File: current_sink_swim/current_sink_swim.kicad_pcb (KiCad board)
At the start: 2 copper layers, 49.3 x 42.6 mm, 23 parts, among them J1 Conn_01x02_Socket, J2 Conn_01x03_Socket, J3 Conn_01x02_Socket, J4 Conn_01x01_Pin, Q2 IRF540N, U1 LMV358, U3 TC1016

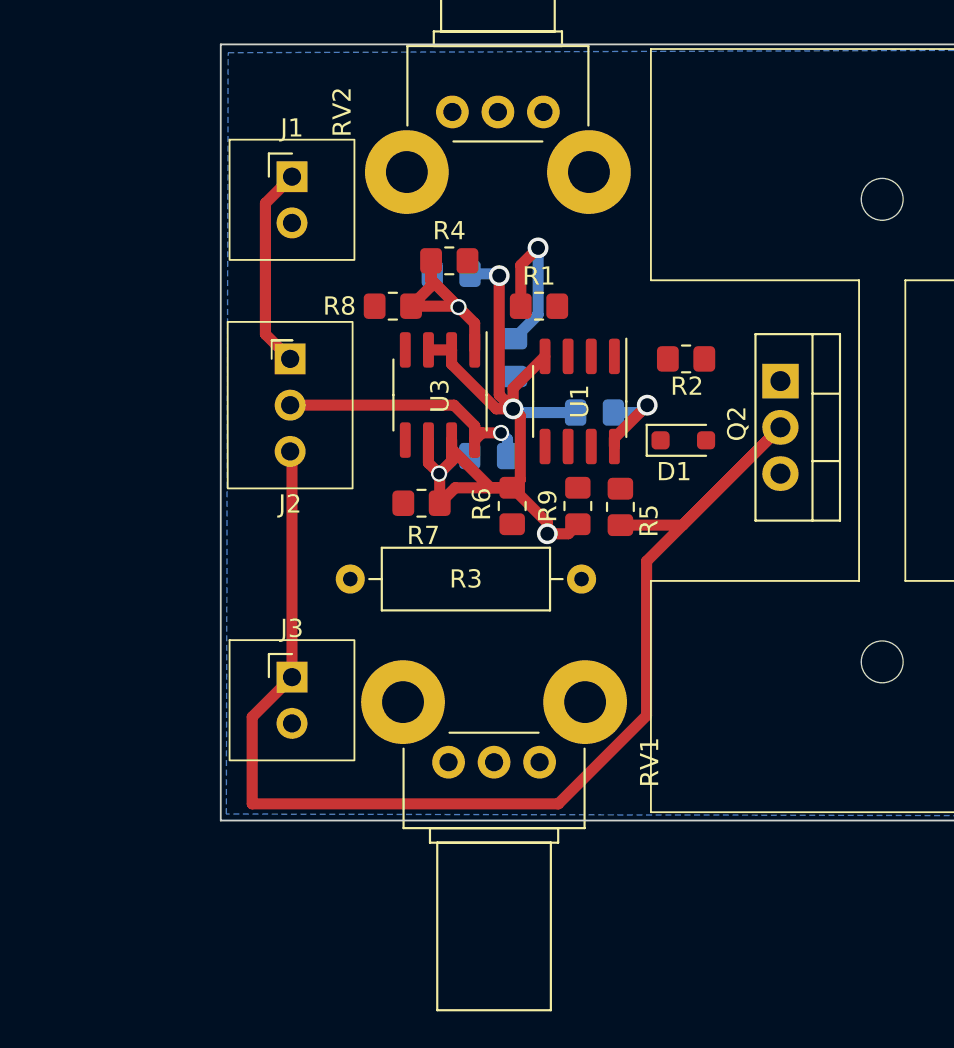
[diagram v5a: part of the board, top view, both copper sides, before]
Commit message: move some componenets around and route all traces
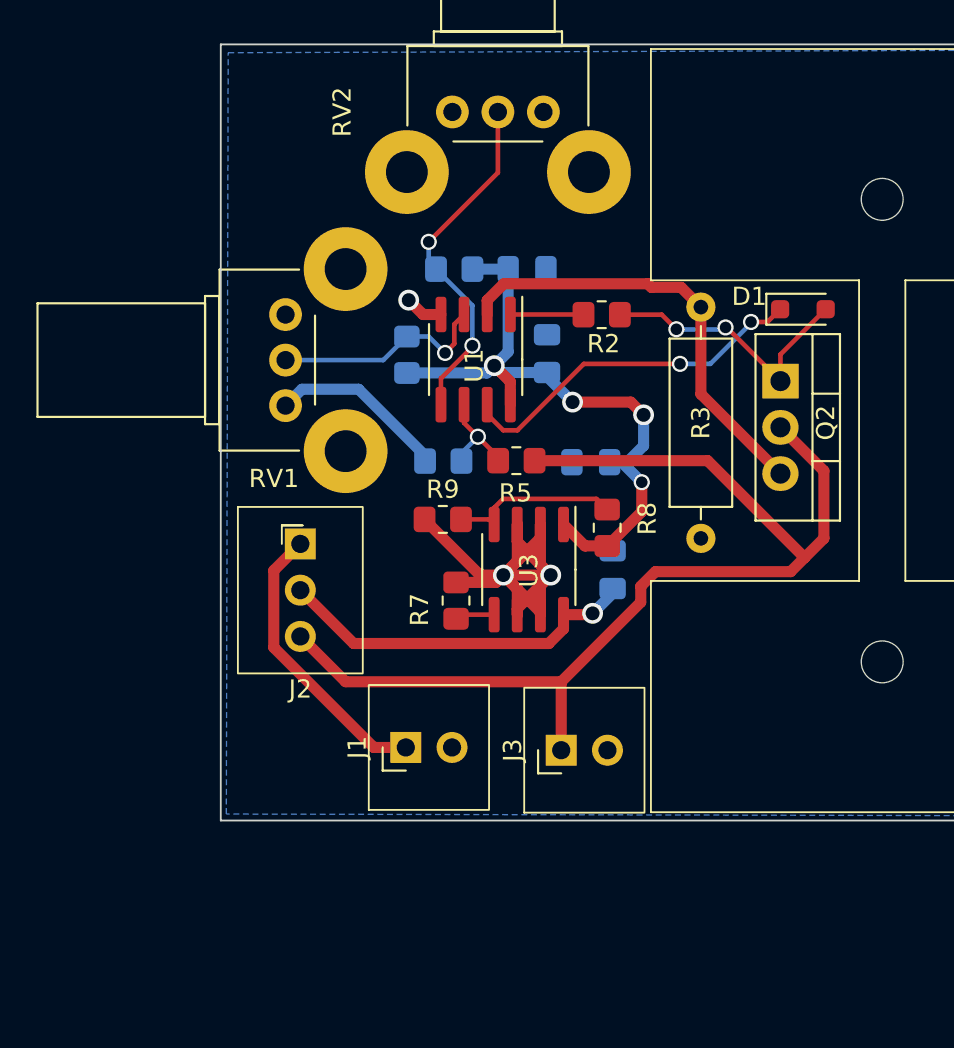
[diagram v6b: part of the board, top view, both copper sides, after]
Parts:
- R1, R4, R6: moved to B.Cu
- moved J1 32.0 mm to (116.9, 67.6), turned to 90 degrees
- moved RV1 26.2 mm to (110.3, 43.8), turned to 180 degrees
- moved R8 16.9 mm to (128.0, 55.5), turned to -90 degrees
- moved R3 16.3 mm to (133.1, 43.4), turned to -90 degrees
- moved J3 15.3 mm to (125.5, 67.7), turned to 90 degrees
- moved U3 10.8 mm to (123.7, 57.8)
- moved J2 10.2 mm to (111.2, 56.4)
- moved D1 9.74 mm to (138.8, 43.5)
- moved C3 9.23 mm to (128.3, 57.8), turned to -90 degrees
- moved R1 7.73 mm to (117.0, 46.0), turned to 90 degrees
- moved R9 7.45 mm to (119.0, 55.0), turned to 0 degrees
- moved C4 7.12 mm to (127.1, 51.9), turned to 0 degrees
- moved R5 6.25 mm to (123.0, 51.8), turned to 180 degrees
- moved U1 6.16 mm to (120.8, 46.3)
- moved R7 5.67 mm to (119.7, 59.5), turned to -90 degrees
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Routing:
- net Net-(Q2-S): track 0.00 -> 24.4 mm
- net Net-(D1-K): track 0.00 -> 19.8 mm, vias 0 -> 2
- net Net-(U1B-+): track 0.00 -> 19.4 mm, vias 0 -> 2
- net / Current Control/FETGate: track 0.00 -> 15.4 mm, vias 0 -> 2
- net Current_Sink+: track 73.9 -> 61.4 mm
- net Net-(U1A-+): track 0.00 -> 12.2 mm, vias 0 -> 1
- net 2.7V: track 28.1 -> 37.8 mm, vias 3 -> 4
- net Net-(U3-ADJ): track 0.00 -> 9.50 mm
- net Vin: track 14.4 -> 20.2 mm
- net Net-(U1B--): track 0.00 -> 5.57 mm, vias 0 -> 1
- net Net-(J1-Pin_1): track 11.2 -> 15.8 mm
- net Current_Sink-: track 51.5 -> 47.0 mm, vias 4 -> 3
- net Net-(R2-Pad1): track 0.00 -> 4.02 mm
- net Net-(U3-INHIBIT): track 0.00 -> 2.19 mm

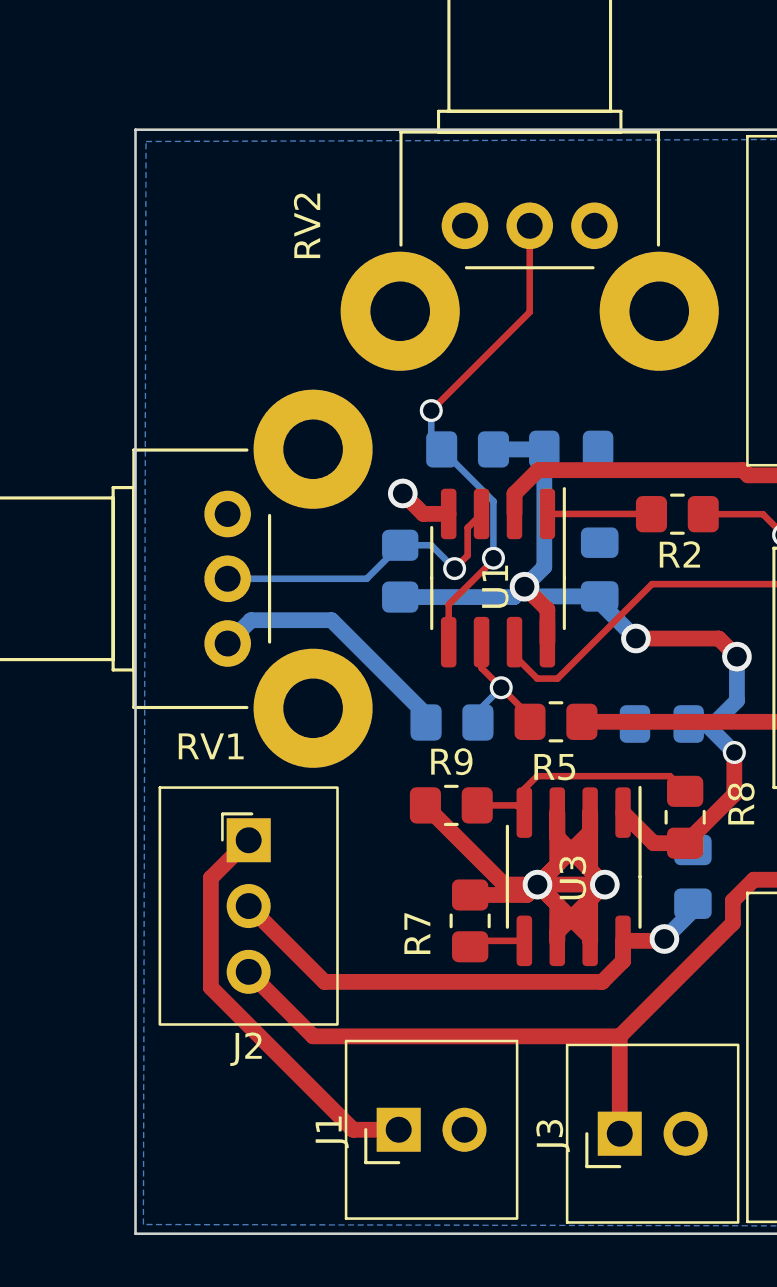
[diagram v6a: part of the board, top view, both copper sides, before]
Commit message: relayed out one resistor
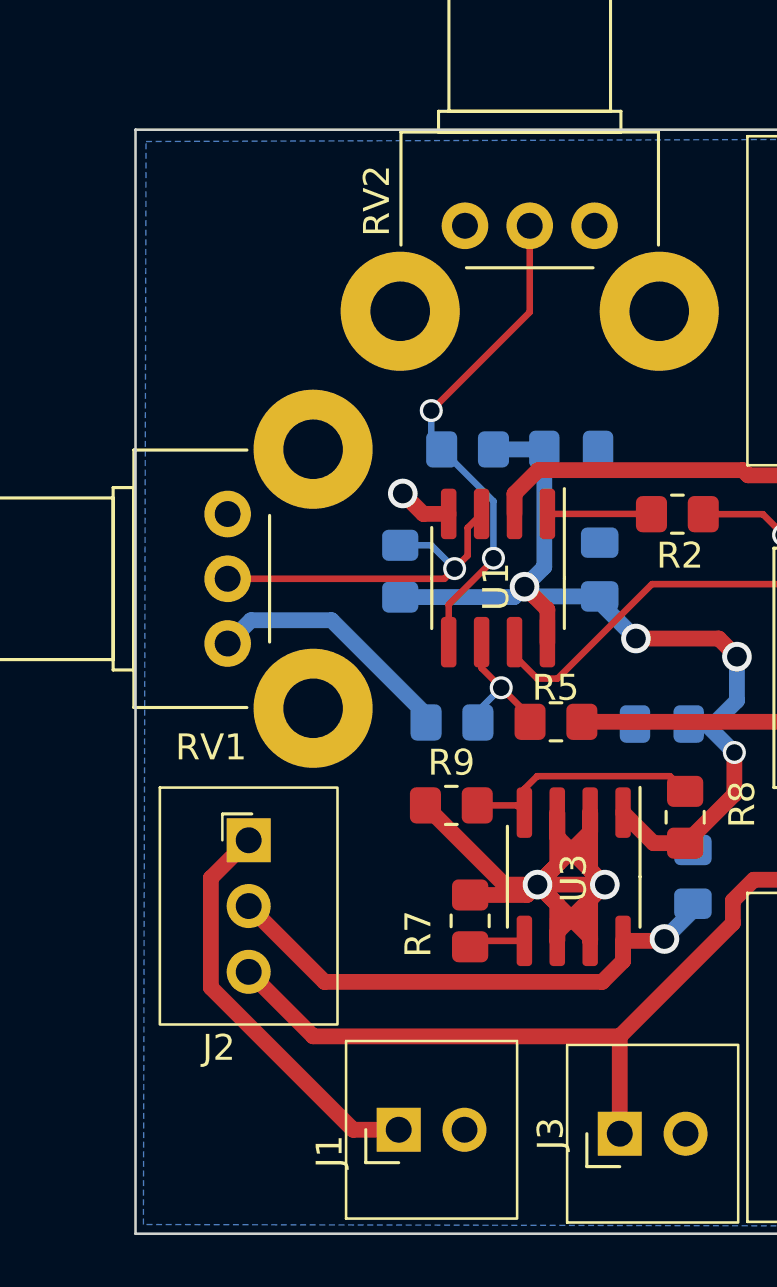
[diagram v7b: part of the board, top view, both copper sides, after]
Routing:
- net Net-(U1A-+): track 12.2 -> 13.9 mm
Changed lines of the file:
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@@
         (effects (font (size 1 1) (thickness 0.15)))
     )
-    (fp_text user "${REFERENCE}" (at -4.3812 -2.221) (layer "F.Fab")
+    (fp_text user "${REFERENCE}" (at -3.2624 -2.1066) (layer "F.Fab")
         (effects (font (size 1 1) (thickness 0.15)))
     )
@@
     (property "ki_keywords" "resistor variable")
     (attr through_hole)
-    (fp_text reference "RV2" (at 0 -11.05 90) (layer "F.SilkS")
+    (fp_text reference "RV2" (at 0.9664 -8.4 90) (layer "F.SilkS")
         (effects (font (size 1 1) (thickness 0.15)))
     )
@@
     (property "ki_keywords" "connector")
     (attr through_hole)
-    (fp_text reference "J2" (at 0 7.9756) (layer "F.SilkS")
+    (fp_text reference "J2" (at -1.1504 8.012) (layer "F.SilkS")
         (effects (font (size 1 1) (thickness 0.15)))
     )
@@
     (property "ki_keywords" "connector")
     (attr through_hole)
-    (fp_text reference "J1" (at 0 -2.667 90) (layer "F.SilkS")
+    (fp_text reference "J1" (at -0.836 -2.667 90) (layer "F.SilkS")
         (effects (font (size 1 1) (thickness 0.15)))
     )
@@
     (property "ki_keywords" "R res resistor")
     (attr smd)
-    (fp_text reference "R5" (at 0.0508 -1.778) (layer "F.SilkS")
+    (fp_text reference "R5" (at 0.0122 1.316) (layer "F.SilkS")
         (effects (font (size 1 1) (thickness 0.15)))
     )
@@
   (segment (start 119.1 45.9) (end 119.6038 45.3962) (width 0.254) (layer "F.Cu") (net 7))
   (segment (start 119.6038 44.3278) (end 120.142 43.7896) (width 0.254) (layer "F.Cu") (net 7))
+  (segment (start 118.7066 46.2934) (end 110.3376 46.2934) (width 0.254) (layer "F.Cu") (net 7))
+  (segment (start 119.1 45.9) (end 118.7066 46.2934) (width 0.254) (layer "F.Cu") (net 7))
   (via (at 119.1 45.9) (size 0.889) (drill 0.635) (layers "F.Cu" "B.Cu") (net 7))
   (segment (start 118.2 45) (end 119.1 45.9) (width 0.254) (layer "B.Cu") (net 7))
-  (segment (start 110.3376 46.2934) (end 115.7066 46.2934) (width 0.254) (layer "B.Cu") (net 7))
-  (segment (start 115.7066 46.2934) (end 117 45) (width 0.254) (layer "B.Cu") (net 7))
   (segment (start 117 45) (end 118.2 45) (width 0.254) (layer "B.Cu") (net 7))
   (segment (start 122.682 43.7896) (end 126.6896 43.7896) (width 0.254) (layer "F.Cu") (net 8))

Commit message: initial generation of gerber files
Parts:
- added G***: LOGO, custom_modules:farm_hacks_logo, F.Cu at (152.1, 49.9)
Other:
- outline, holes or cut-outs redrawn
- board text added: "Current Sink or Swim"
